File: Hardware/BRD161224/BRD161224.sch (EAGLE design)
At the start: 16 parts, among them Q1 DMP2035, Q2 FDV301, Q3 FDV301, Q4 DMP2035, Q5 DMP2035, Q6 DMP2035

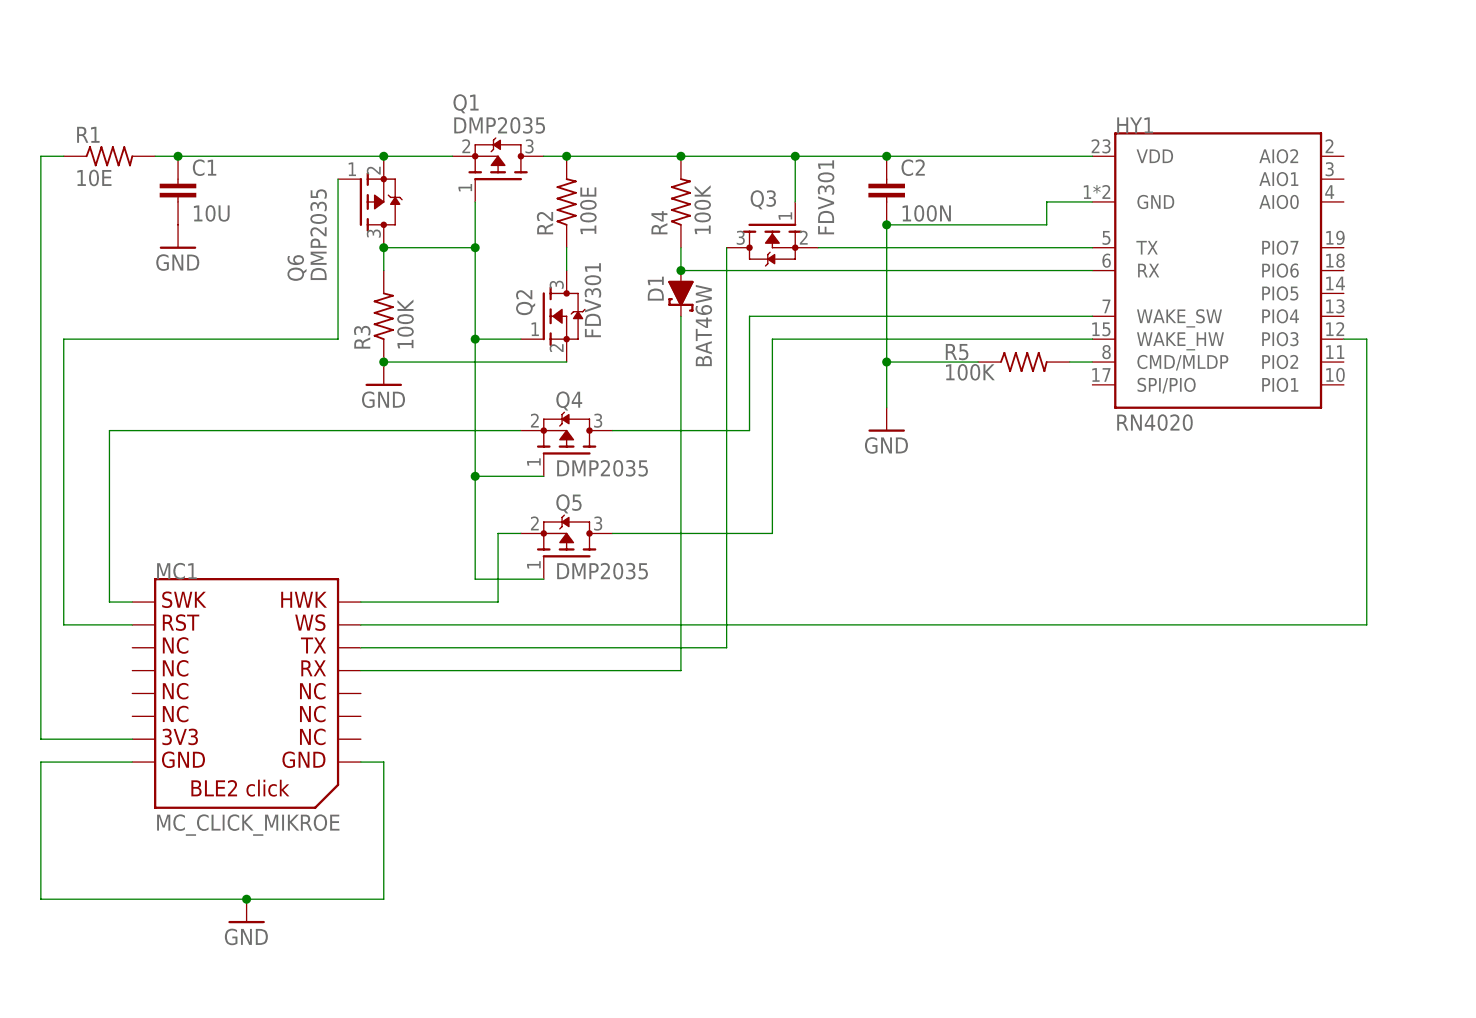
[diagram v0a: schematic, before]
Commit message: ble2_click R00 finished
Signed-off-by: Christoph Tack <prog.send@gmail.com>
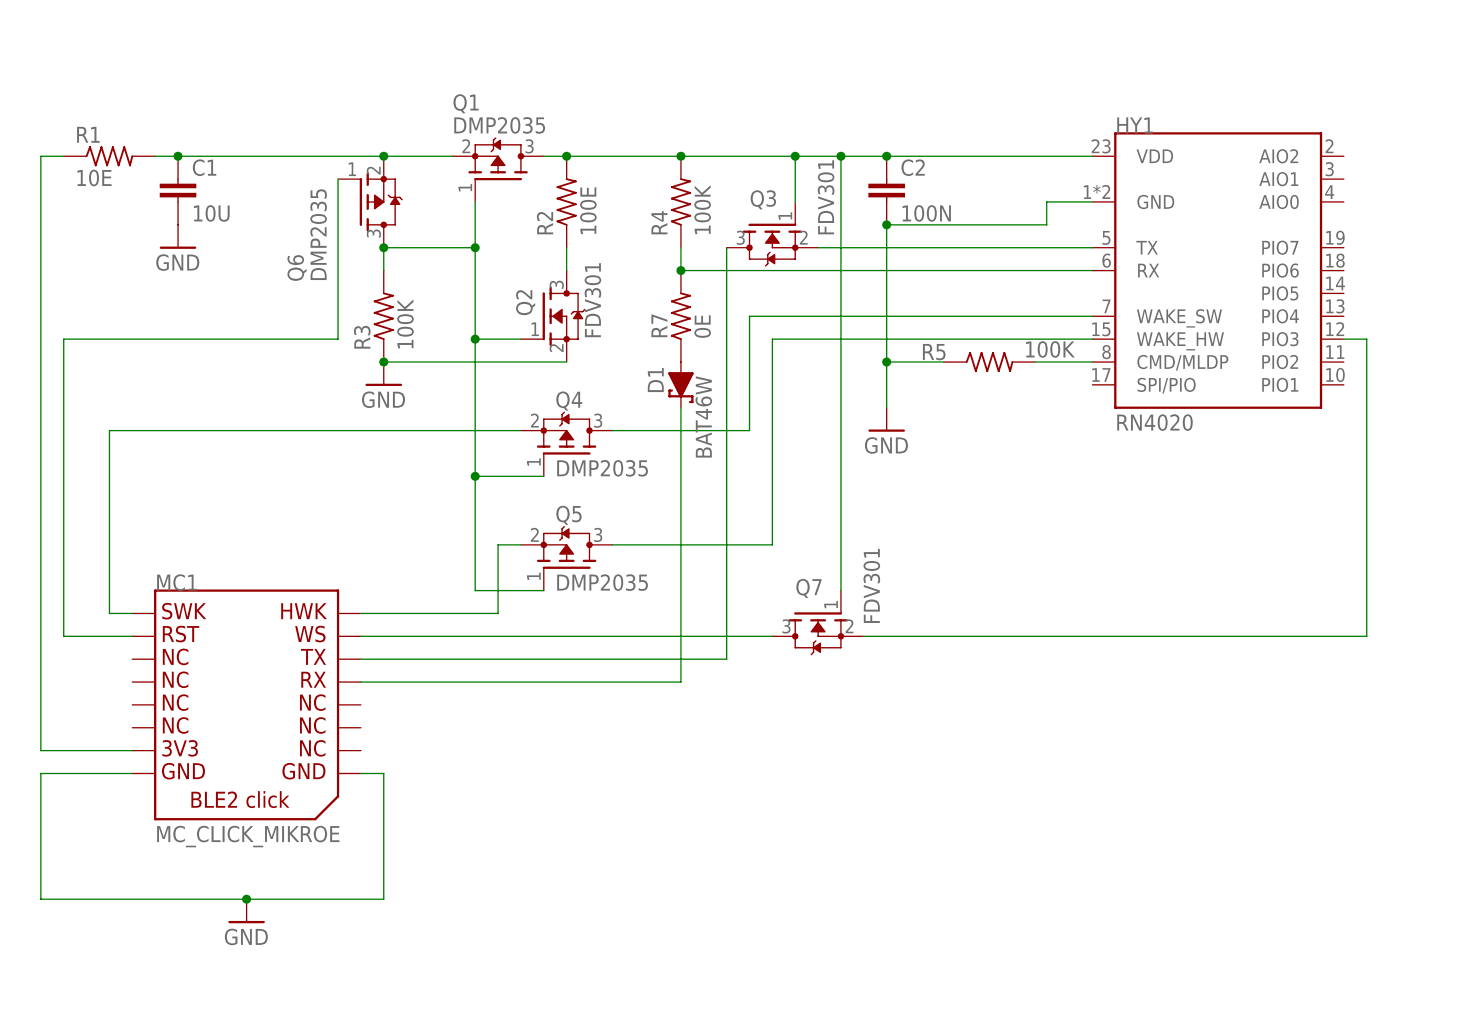
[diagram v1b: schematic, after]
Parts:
- added Q7: FDV301, lieBtrau:TR_NMOS_FDV301_SOT23
- added R7: 0E, lieBtrau:RE_0E_1206
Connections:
- new net N$16: HY1.RX, R4.1, R7.2
- new net N$18: MC1.P$15, Q7.D
- net N$11: now also Q7.S; no longer MC1.P$15
- net N$2: now also Q7.G
- net N$8: now also R7.1; no longer HY1.RX, R4.1
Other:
- moved on the sheet: D1, MC1, Q5, R5

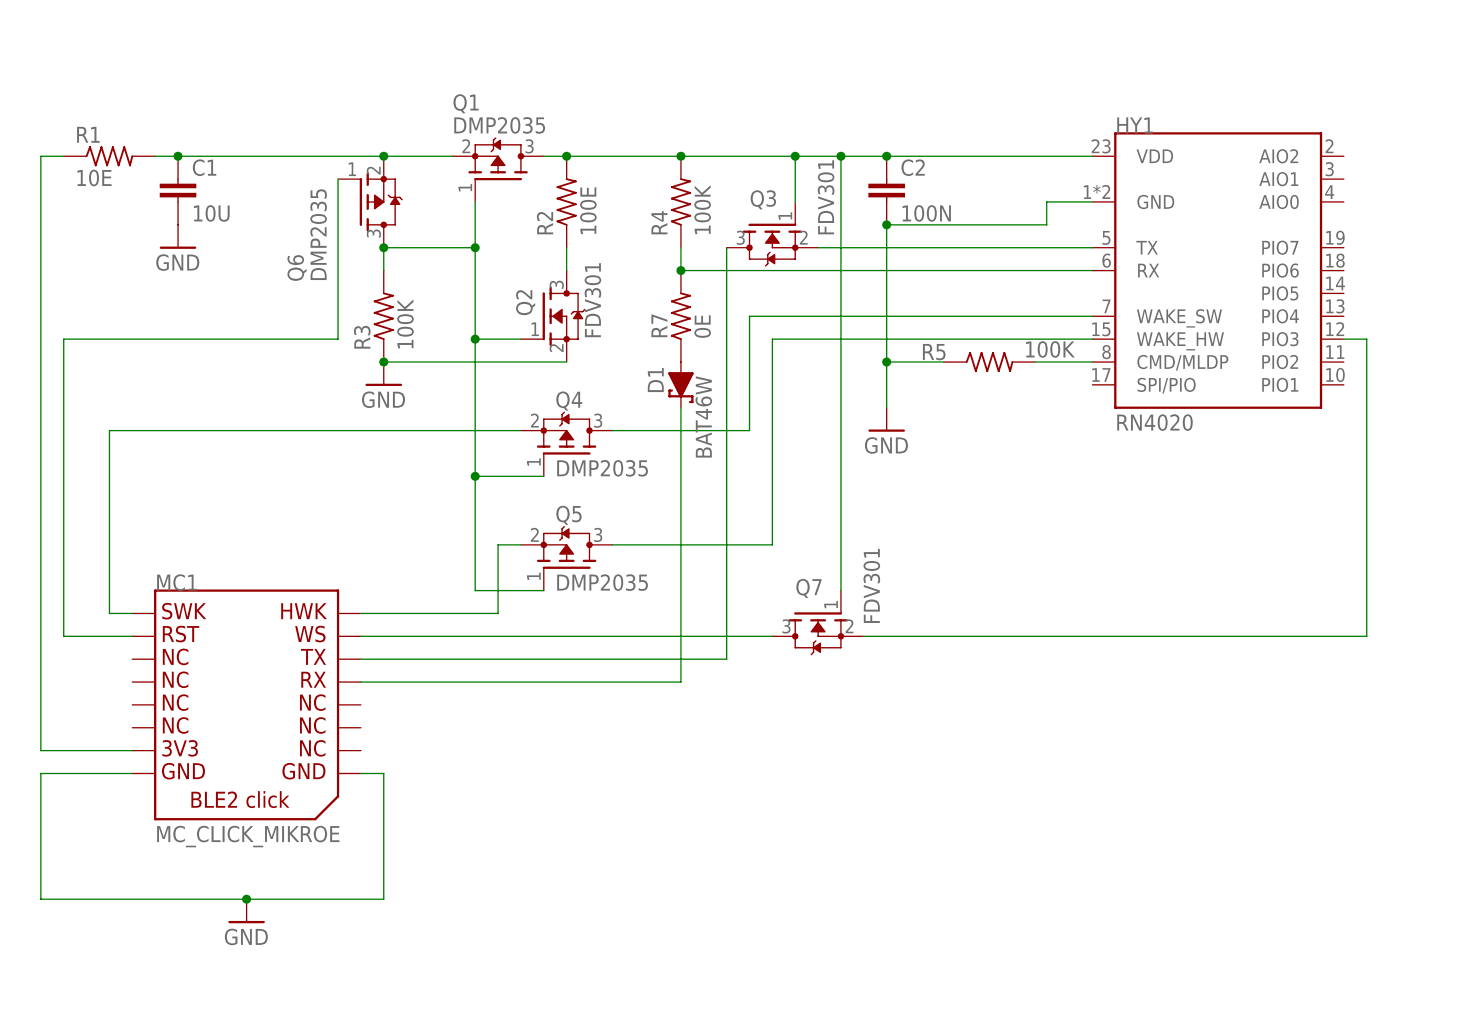
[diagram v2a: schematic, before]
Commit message: Schematic: replacing D1, R7 and R4 by Q8.
Signed-off-by: Christoph Tack <prog.send@gmail.com>
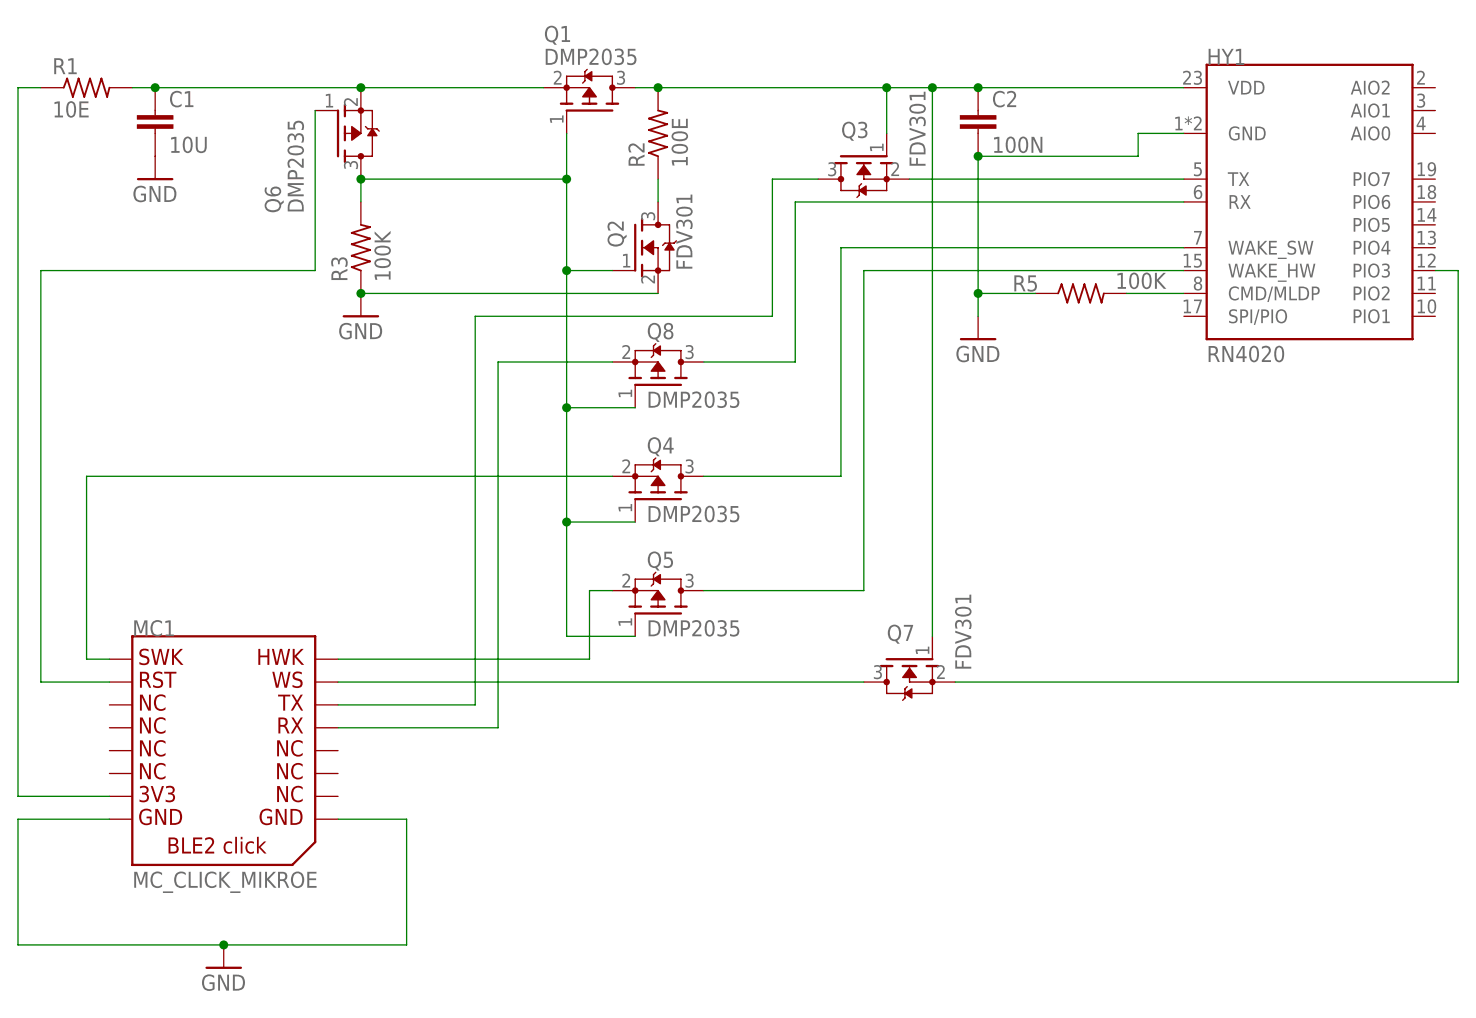
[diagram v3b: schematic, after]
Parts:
- removed D1: BAT46W, lieBtrau:DI_SCHOTTKY_BAT46W_SOD323
- removed R4: 100K, lieBtrau:RE_100K_1206
- removed R7: 0E, lieBtrau:RE_0E_1206
- added Q8: DMP2035, lieBtrau:TR_PMOS_DMP2035_SOT23
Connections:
- removed net N$9 (its old number): D1.C, MC1.P$13
- net N$16: now also Q8.D; no longer R4.1, R7.2
- net N$2: no longer R4.2
- net N$4: now also Q8.G
- net N$8: now also MC1.P$13, Q8.S; no longer D1.A, R7.1
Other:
- moved on the sheet: C1, C2, HY1, MC1, Q1, Q2, Q3, Q4, Q5, Q6, Q7, R1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
